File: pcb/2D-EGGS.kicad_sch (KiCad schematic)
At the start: 40 parts, among them J1 BUTTON 1, J10 EFFECT, J11 AUX, J12 USB_B, J13 PWAN1, J14 PWAN2, J15 ENCODER, J2 BUTTON 2, J3 BUTTON 3, J4 BUTTON 4, J5 BUTTON 5, J6 BUTTON 6, J7 BUTTON 7, J8 START, J9 VEFX, Q1 2N7000, Q10 2N7000, Q11 2N7000, Q2 2N7000, Q3 2N7000, Q4 2N7000, Q5 2N7000, Q6 2N7000, Q7 2N7000, Q8 2N7000, Q9 2N7000, SW1 SW_Push, U1 AT90USB1286, Y1 16MHz

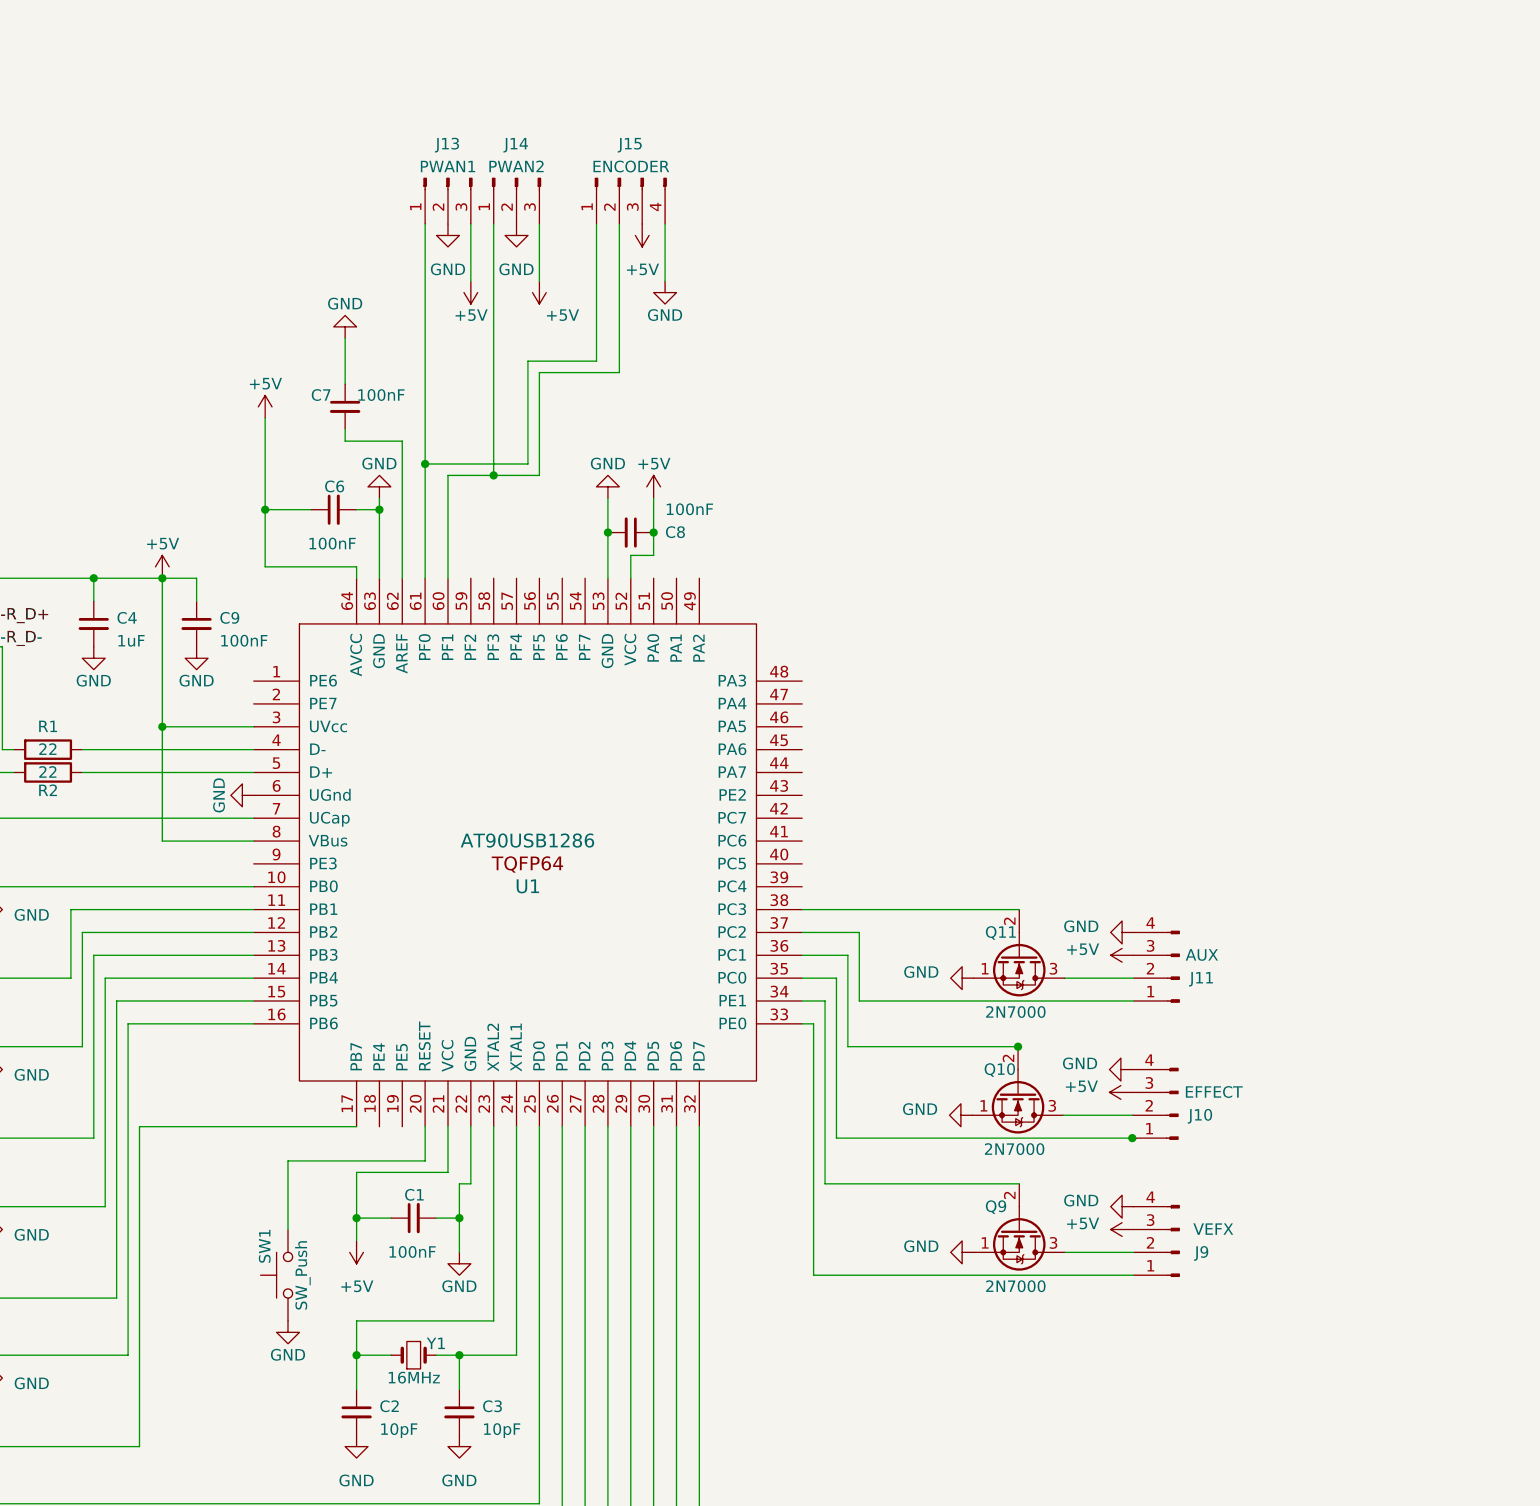
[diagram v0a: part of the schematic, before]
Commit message: wire unused pins to 24-pin connector
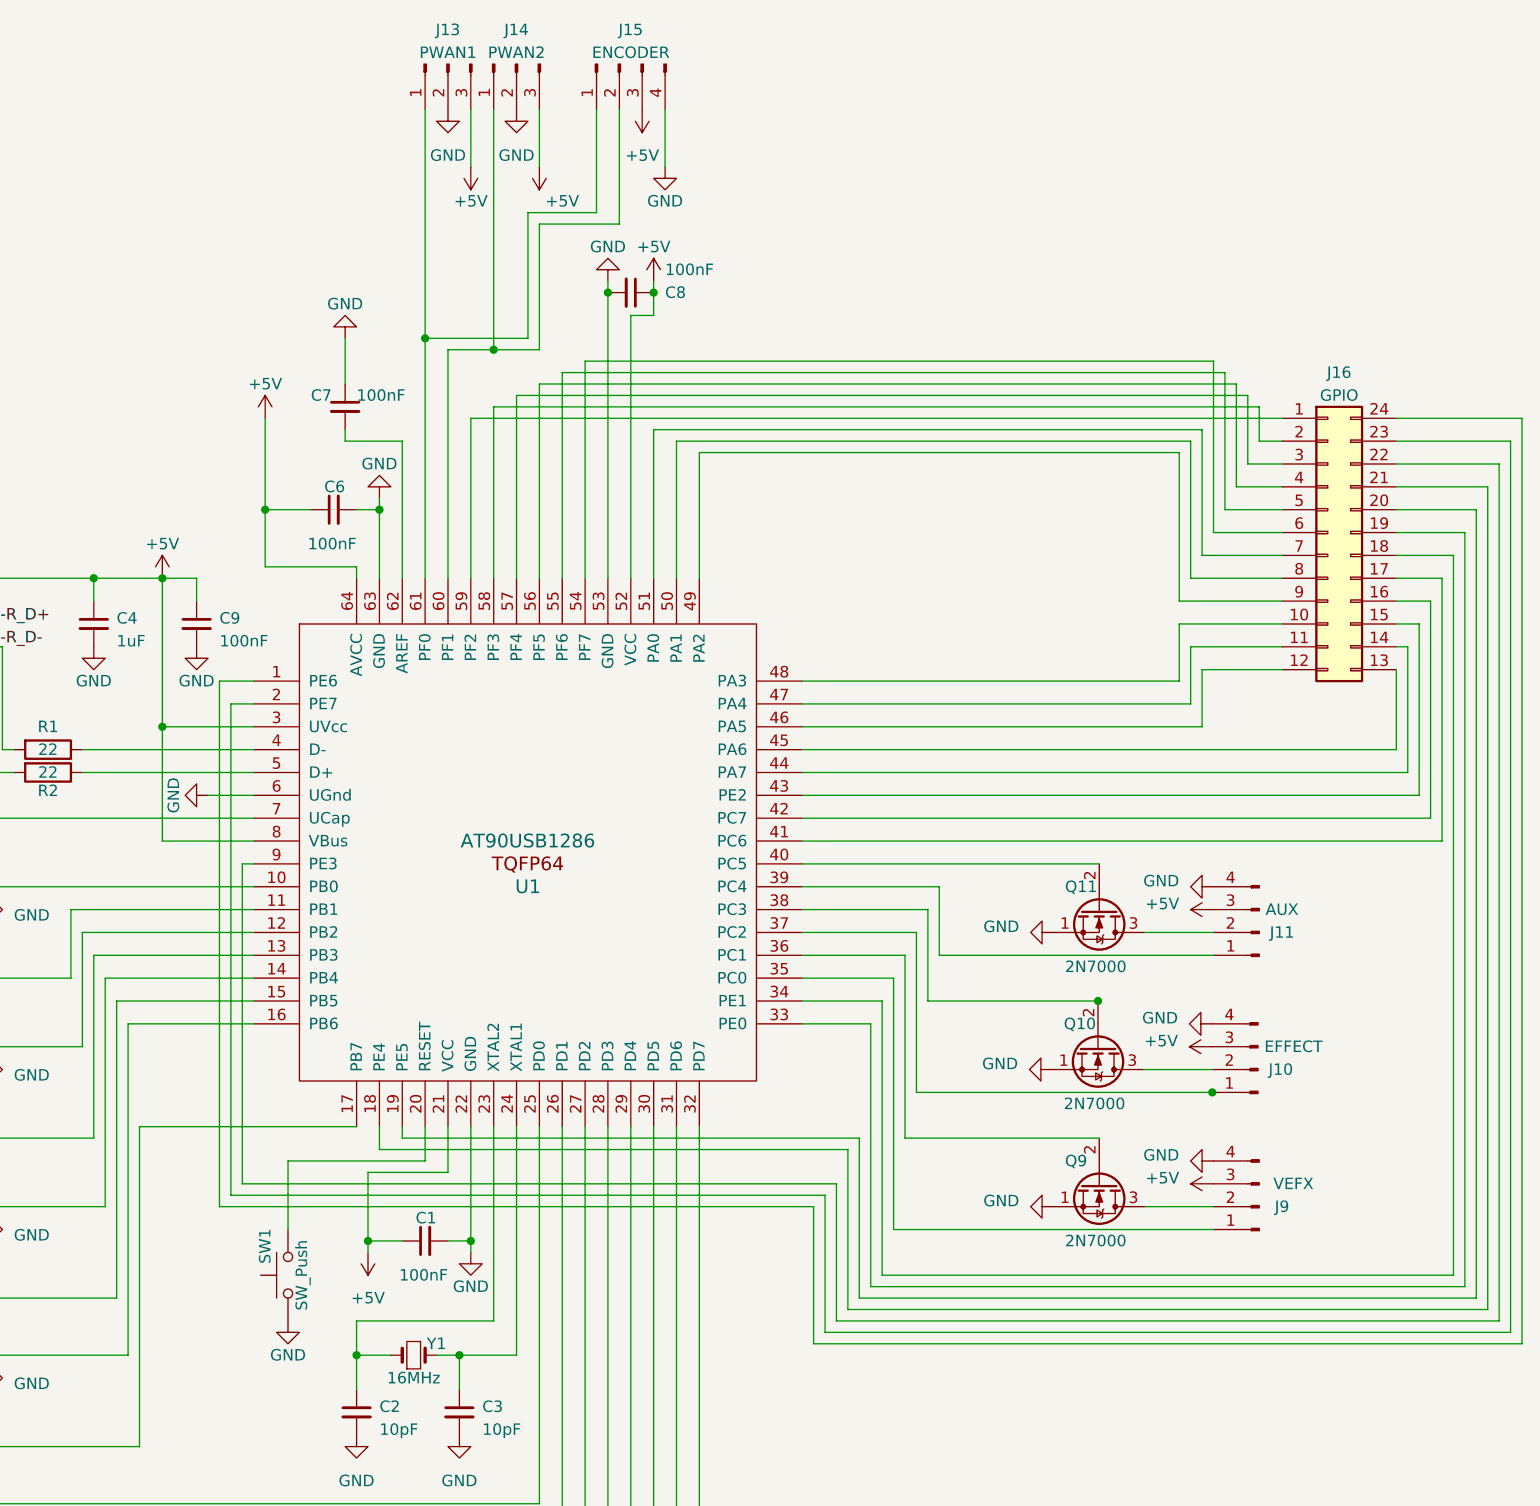
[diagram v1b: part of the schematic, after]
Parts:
- added J16: GPIO, symbol Connector_Generic:Conn_02x12_Counter_Clockwise
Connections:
- net at Q10.2 (G): now also U1.38 (PC3); no longer U1.36 (PC1)
- net at Q11.2 (G): now also U1.40 (PC5); no longer U1.38 (PC3)
- net at J9.1 (Pin_1): now also U1.35 (PC0); no longer U1.33 (PE0)
- net at U1.1 (PE6): now also J16.24 (Pin_24)
- net at U1.18 (PE4): now also J16.21 (Pin_21)
- net at U1.19 (PE5): now also J16.20 (Pin_20)
- net at U1.2 (PE7): now also J16.23 (Pin_23)
- net at U1.34 (PE1): now also J16.18 (Pin_18); no longer Q9.2 (G)
- net at J10.1 (Pin_1): now also U1.37 (PC2); no longer U1.35 (PC0)
- net at J11.1 (Pin_1): now also U1.39 (PC4); no longer U1.37 (PC2)
- net at U1.41 (PC6): now also J16.17 (Pin_17)
- net at U1.42 (PC7): now also J16.16 (Pin_16)
- net at U1.43 (PE2): now also J16.15 (Pin_15)
- net at U1.44 (PA7): now also J16.14 (Pin_14)
- net at U1.45 (PA6): now also J16.13 (Pin_13)
- net at U1.46 (PA5): now also J16.12 (Pin_12)
- net at U1.47 (PA4): now also J16.11 (Pin_11)
- net at U1.48 (PA3): now also J16.10 (Pin_10)
- net at U1.49 (PA2): now also J16.9 (Pin_9)
- net at U1.50 (PA1): now also J16.8 (Pin_8)
- net at U1.51 (PA0): now also J16.7 (Pin_7)
- net at U1.54 (PF7): now also J16.6 (Pin_6)
- net at U1.55 (PF6): now also J16.5 (Pin_5)
- net at U1.56 (PF5): now also J16.4 (Pin_4)
- net at U1.57 (PF4): now also J16.3 (Pin_3)
- net at U1.58 (PF3): now also J16.2 (Pin_2)
- net at U1.59 (PF2): now also J16.1 (Pin_1)
- net at U1.9 (PE3): now also J16.22 (Pin_22)
- new net: J16.19 (Pin_19), U1.33 (PE0)
- new net: Q9.2 (G), U1.36 (PC1)
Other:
- moved on the sheet: C1, C8, J10, J11, J13, J14, J15, J9, Q10, Q11, Q9

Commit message: rough pcb layout, remove auto_saved_files
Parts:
- C1, C2, C3, C4, C5, C6, C7, C8, C9: footprint (none) -> Capacitor_SMD:C_0805_2012Metric
- J1, J10, J11, J15, J2, J3, J4, J5, J6, J7, J8, J9: footprint (none) -> Connector_JST:JST_XH_B4B-XH-A_1x04_P2.50mm_Vertical
- J12: footprint footprints:USB_B_OST_USB-B1HSxx_Horizontal -> Connector_USB:USB_B_OST_USB-B1HSxx_Horizontal
- J13, J14: footprint (none) -> Connector_JST:JST_XH_B3B-XH-A_1x03_P2.50mm_Vertical
- J16: footprint (none) -> Connector_PinHeader_2.54mm:PinHeader_2x12_P2.54mm_Vertical
- R1, R2: footprint footprints:R_0805_2012Metric -> Resistor_SMD:R_0805_2012Metric
- SW1: footprint footprints:BUTTON -> Button_Switch_THT:SW_PUSH_6mm
- U1: footprint (none) -> Package_QFP:TQFP-64_14x14mm_P0.8mm
- Y1: footprint footprints:Crystal_SMD_SeikoEpson_FA238-4Pin_3.2x2.5mm -> Crystal:Crystal_HC49-4H_Vertical
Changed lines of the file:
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@@
       (effects (font (size 1.27 1.27)))
     )
-    (property "Footprint" "" (at 102.87 214.63 0)
+    (property "Footprint" "Connector_JST:JST_XH_B4B-XH-A_1x04_P2.50mm_Vertical" (at 102.87 214.63 0)
       (effects (font (size 1.27 1.27)) hide)
     )
@@
       (effects (font (size 1.27 1.27)) (justify left))
     )
-    (property "Footprint" "" (at 138.43 82.55 0)
+    (property "Footprint" "Capacitor_SMD:C_0805_2012Metric" (at 138.43 82.55 0)
       (effects (font (size 1.27 1.27)) hide)
     )
@@
       (effects (font (size 1.27 1.27)))
     )
-    (property "Footprint" "" (at 102.87 132.08 0)
+    (property "Footprint" "Connector_JST:JST_XH_B4B-XH-A_1x04_P2.50mm_Vertical" (at 102.87 132.08 0)
       (effects (font (size 1.27 1.27)) hide)
     )
@@
       (effects (font (size 1.27 1.27)))
     )
-    (property "Footprint" "" (at 102.87 198.12 0)
+    (property "Footprint" "Connector_JST:JST_XH_B4B-XH-A_1x04_P2.50mm_Vertical" (at 102.87 198.12 0)
       (effects (font (size 1.27 1.27)) hide)
     )
@@
       (effects (font (size 1.27 1.27)))
     )
-    (property "Footprint" "" (at 123.19 104.14 0)
+    (property "Footprint" "Capacitor_SMD:C_0805_2012Metric" (at 123.19 104.14 0)
       (effects (font (size 1.27 1.27)) hide)
     )
@@
       (effects (font (size 1.27 1.27)))
     )
-    (property "Footprint" "" (at 102.87 149.86 0)
+    (property "Footprint" "Connector_JST:JST_XH_B4B-XH-A_1x04_P2.50mm_Vertical" (at 102.87 149.86 0)
       (effects (font (size 1.27 1.27)) hide)
     )
@@
       (effects (font (size 1.27 1.27)))
     )
-    (property "Footprint" "" (at 177.8 20.32 0)
+    (property "Footprint" "Connector_JST:JST_XH_B3B-XH-A_1x03_P2.50mm_Vertical" (at 177.8 20.32 0)
       (effects (font (size 1.27 1.27)) hide)
     )
@@
       (effects (font (size 1.27 1.27)))
     )
-    (property "Footprint" "" (at 102.87 166.37 0)
+    (property "Footprint" "Connector_JST:JST_XH_B4B-XH-A_1x04_P2.50mm_Vertical" (at 102.87 166.37 0)
       (effects (font (size 1.27 1.27)) hide)
     )
@@
       (effects (font (size 1.27 1.27)))
     )
-    (property "Footprint" "footprints:Crystal_SMD_SeikoEpson_FA238-4Pin_3.2x2.5mm" (at 173.99 163.83 0)
+    (property "Footprint" "Crystal:Crystal_HC49-4H_Vertical" (at 173.99 163.83 0)
       (effects (font (size 1.27 1.27)) hide)
     )
@@
       (effects (font (size 1.27 1.27)))
     )
-    (property "Footprint" "" (at 196.85 20.32 0)
+    (property "Footprint" "Connector_JST:JST_XH_B4B-XH-A_1x04_P2.50mm_Vertical" (at 196.85 20.32 0)
       (effects (font (size 1.27 1.27)) hide)
     )
@@
       (effects (font (size 1.27 1.27)))
     )
-    (property "Footprint" "" (at 267.97 147.32 0)
+    (property "Footprint" "Connector_JST:JST_XH_B4B-XH-A_1x04_P2.50mm_Vertical" (at 267.97 147.32 0)
       (effects (font (size 1.27 1.27)) hide)
     )
@@
       (effects (font (size 1.524 1.524)))
     )
-    (property "Footprint" "" (at 168.91 100.33 0)
+    (property "Footprint" "Package_QFP:TQFP-64_14x14mm_P0.8mm" (at 168.91 100.33 0)
       (effects (font (size 1.524 1.524)) hide)
     )
@@
       (effects (font (size 1.27 1.27)))
     )
-    (property "Footprint" "footprints:R_0805_2012Metric" (at 133.35 94.742 90)
+    (property "Footprint" "Resistor_SMD:R_0805_2012Metric" (at 133.35 94.742 90)
       (effects (font (size 1.27 1.27)) hide)
     )
@@
       (effects (font (size 1.27 1.27)) (justify left))
     )
-    (property "Footprint" "" (at 167.64 170.18 0)
+    (property "Footprint" "Capacitor_SMD:C_0805_2012Metric" (at 167.64 170.18 0)
       (effects (font (size 1.27 1.27)) hide)
     )
@@
       (effects (font (size 1.27 1.27)) (justify left))
     )
-    (property "Footprint" "" (at 179.07 170.18 0)
+    (property "Footprint" "Capacitor_SMD:C_0805_2012Metric" (at 179.07 170.18 0)
       (effects (font (size 1.27 1.27)) hide)
     )
@@
       (effects (font (size 1.27 1.27)) (justify left))
     )
-    (property "Footprint" "" (at 198.12 45.72 0)
+    (property "Footprint" "Capacitor_SMD:C_0805_2012Metric" (at 198.12 45.72 0)
       (effects (font (size 1.27 1.27)) hide)
     )
@@
       (effects (font (size 1.27 1.27)))
     )
-    (property "Footprint" "footprints:R_0805_2012Metric" (at 133.35 97.282 90)
+    (property "Footprint" "Resistor_SMD:R_0805_2012Metric" (at 133.35 97.282 90)
       (effects (font (size 1.27 1.27)) hide)
     )
@@
       (effects (font (size 1.27 1.27)) (justify left))
     )
-    (property "Footprint" "" (at 149.86 82.55 0)
+    (property "Footprint" "Capacitor_SMD:C_0805_2012Metric" (at 149.86 82.55 0)
       (effects (font (size 1.27 1.27)) hide)
     )
@@
       (effects (font (size 1.27 1.27)))
     )
-    (property "Footprint" "" (at 275.59 72.39 0)
+    (property "Footprint" "Connector_PinHeader_2.54mm:PinHeader_2x12_P2.54mm_Vertical" (at 275.59 72.39 0)
       (effects (font (size 1.27 1.27)) hide)
     )
@@
       (effects (font (size 1.27 1.27)) (justify left))
     )
-    (property "Footprint" "" (at 175.26 151.13 0)
+    (property "Footprint" "Capacitor_SMD:C_0805_2012Metric" (at 175.26 151.13 0)
       (effects (font (size 1.27 1.27)) hide)
     )
@@
       (effects (font (size 1.27 1.27)) (justify left))
     )
-    (property "Footprint" "" (at 165.1 69.85 0)
+    (property "Footprint" "Capacitor_SMD:C_0805_2012Metric" (at 165.1 69.85 0)
       (effects (font (size 1.27 1.27)) hide)
     )
@@
       (effects (font (size 1.27 1.27)))
     )
-    (property "Footprint" "footprints:USB_B_OST_USB-B1HSxx_Horizontal" (at 120.65 83.82 0)
+    (property "Footprint" "Connector_USB:USB_B_OST_USB-B1HSxx_Horizontal" (at 120.65 83.82 0)
       (effects (font (size 1.27 1.27)) hide)
     )
@@
       (effects (font (size 1.27 1.27)))
     )
-    (property "Footprint" "footprints:BUTTON" (at 154.94 154.94 0)
+    (property "Footprint" "Button_Switch_THT:SW_PUSH_6mm" (at 154.94 154.94 0)
       (effects (font (size 1.27 1.27)) hide)
     )
@@
       (effects (font (size 1.27 1.27)))
     )
-    (property "Footprint" "" (at 185.42 20.32 0)
+    (property "Footprint" "Connector_JST:JST_XH_B3B-XH-A_1x03_P2.50mm_Vertical" (at 185.42 20.32 0)
       (effects (font (size 1.27 1.27)) hide)
     )
@@
       (effects (font (size 1.27 1.27)))
     )
-    (property "Footprint" "" (at 267.97 116.84 0)
+    (property "Footprint" "Connector_JST:JST_XH_B4B-XH-A_1x04_P2.50mm_Vertical" (at 267.97 116.84 0)
       (effects (font (size 1.27 1.27)) hide)
     )
@@
       (effects (font (size 1.27 1.27)) (justify left))
     )
-    (property "Footprint" "" (at 166.37 58.42 0)
+    (property "Footprint" "Capacitor_SMD:C_0805_2012Metric" (at 166.37 58.42 0)
       (effects (font (size 1.27 1.27)) hide)
     )
@@
       (effects (font (size 1.27 1.27)))
     )
-    (property "Footprint" "" (at 102.87 114.3 0)
+    (property "Footprint" "Connector_JST:JST_XH_B4B-XH-A_1x04_P2.50mm_Vertical" (at 102.87 114.3 0)
       (effects (font (size 1.27 1.27)) hide)
     )
@@
       (effects (font (size 1.27 1.27)))
     )
-    (property "Footprint" "" (at 102.87 182.88 0)
+    (property "Footprint" "Connector_JST:JST_XH_B4B-XH-A_1x04_P2.50mm_Vertical" (at 102.87 182.88 0)
       (effects (font (size 1.27 1.27)) hide)
     )
@@
       (effects (font (size 1.27 1.27)))
     )
-    (property "Footprint" "" (at 102.87 231.14 0)
+    (property "Footprint" "Connector_JST:JST_XH_B4B-XH-A_1x04_P2.50mm_Vertical" (at 102.87 231.14 0)
       (effects (font (size 1.27 1.27)) hide)
     )
@@
       (effects (font (size 1.27 1.27)))
     )
-    (property "Footprint" "" (at 267.834 132.08 0)
-      (effects (font (size 1.27 1.27)) hide)
-    )
+    (property "Footprint" "Connector_JST:JST_XH_B4B-XH-A_1x04_P2.50mm_Vertical" (at 267.834 132.08 0)
+      (effects (font (size 1.27 1.27)) hide)
+    )

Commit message: routing done
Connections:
- net MCU_D-: now reaches R1.1, U1.4 (D-)
- net MCU_D+: now reaches R2.1, U1.5 (D+)
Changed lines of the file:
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@@
     (stroke (width 0) (type default))
+  )
+  (label "MCU_D-" (at 137.16 96.52 0) (fields_autoplaced)
+    (effects (font (size 1.27 1.27)) (justify left bottom))
   )
   (label "USB-R_D-" (at 124.46 85.09 0) (fields_autoplaced)
     (effects (font (size 1.27 1.27)) (justify left bottom))
   )
+  (label "MCU_D+" (at 137.16 99.06 0) (fields_autoplaced)
+    (effects (font (size 1.27 1.27)) (justify left bottom))
+  )
